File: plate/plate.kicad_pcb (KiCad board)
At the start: 2 copper layers, 285.8 x 105.3 mm, 0 parts

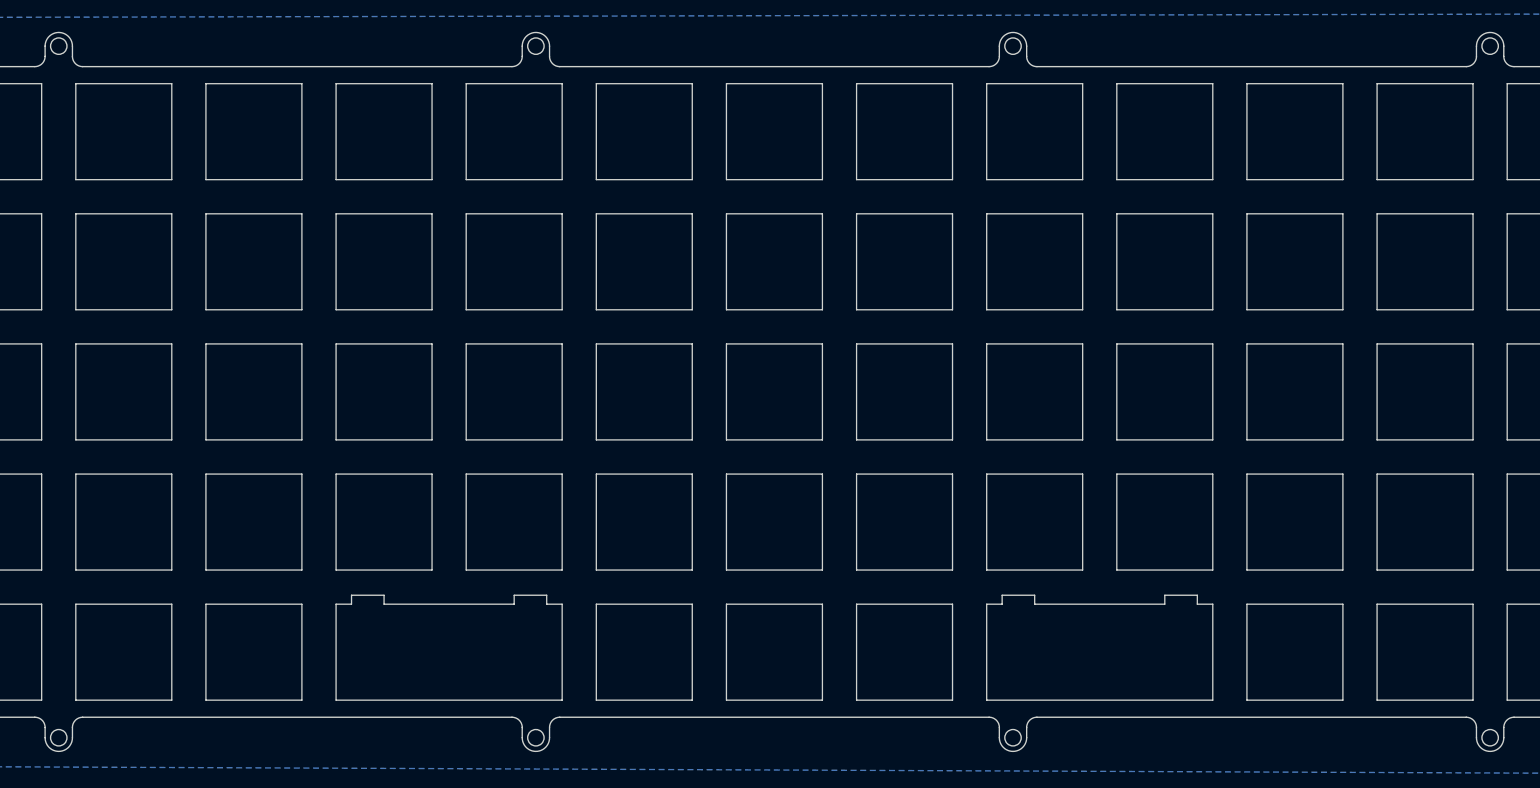
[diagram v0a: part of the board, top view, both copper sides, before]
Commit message: Add stab cutouts to plate
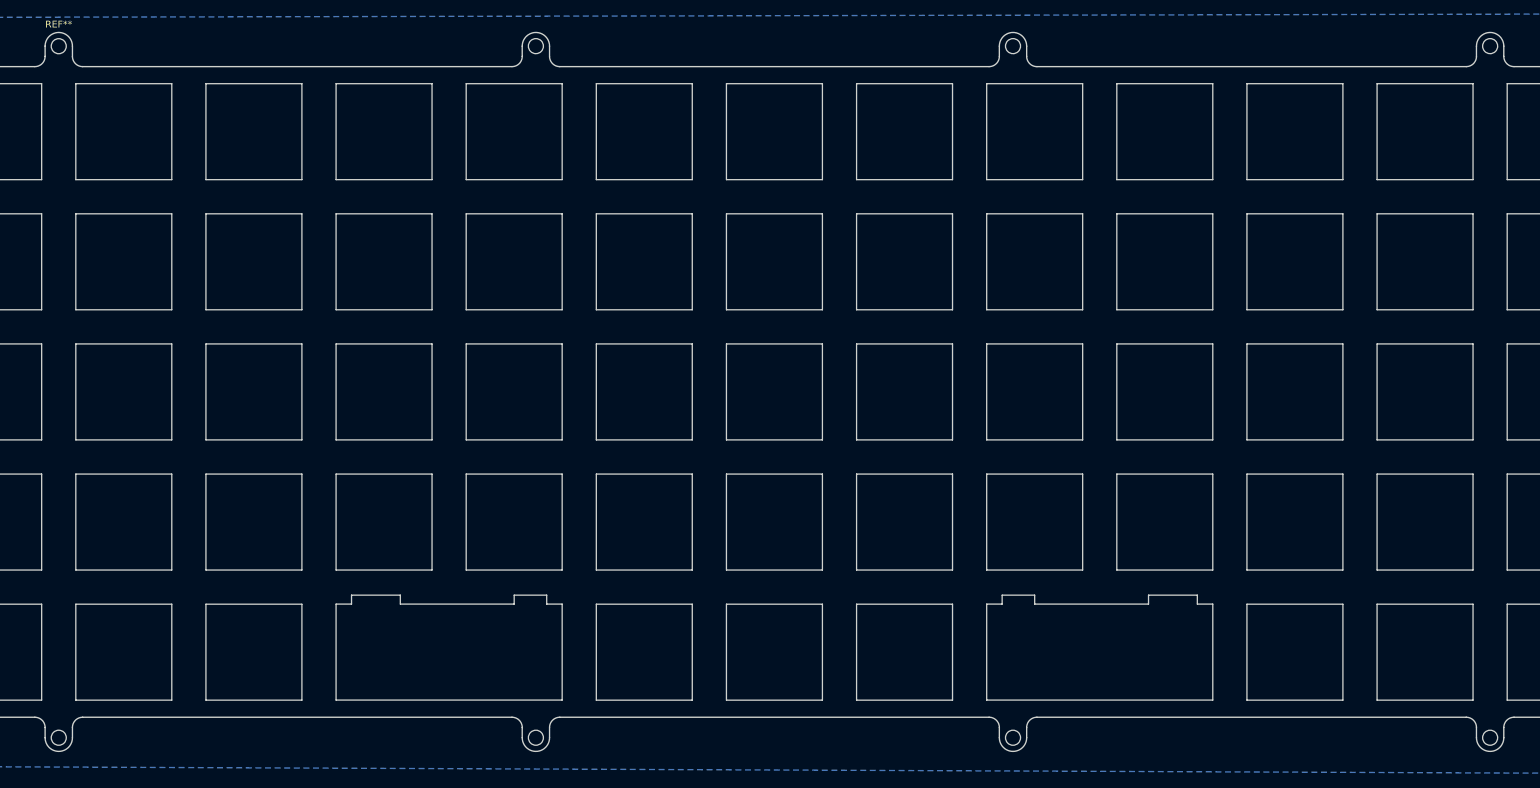
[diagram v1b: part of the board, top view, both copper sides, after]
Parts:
- added ?: , , F.Cu at (239.9, 45.2)
- added ?: , , F.Cu at (170.1, 146.5)
- added ?: , , F.Cu at (239.9, 146.5)
- added ?: , , F.Cu at (170.1, 45.2)
- added ?: , , F.Cu at (100.2, 45.2)
- added ?: , , F.Cu at (100.2, 146.5)
- added ?: , , F.Cu at (30.4, 146.5)
- added REF**: MountingHole_2.2mm_M2, MountingHole:MountingHole_2.2mm_M2, F.Cu at (30.4, 45.2)
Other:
- outline, holes or cut-outs redrawn
